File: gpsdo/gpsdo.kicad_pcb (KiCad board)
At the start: 4 copper layers, 100 x 100 mm, 64 parts, among them J1 Conn_02x05_Odd_Even, J2 Barrel_Jack_Switch, J4 USB_B_Micro, J5 Conn_01x02_Male, SW1 pushbutton_switch, SW2 SW_SPDT, U1 STM32F407VETx, U2 ATGM336H-5N, U3 AP1117-33, U4 74AHC1G04-newfp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

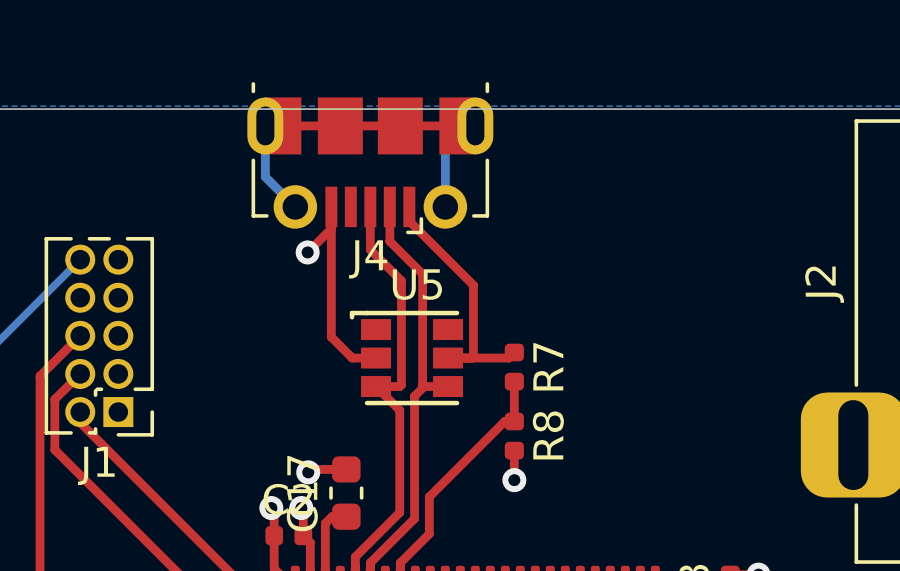
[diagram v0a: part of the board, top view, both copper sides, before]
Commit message: usb connector
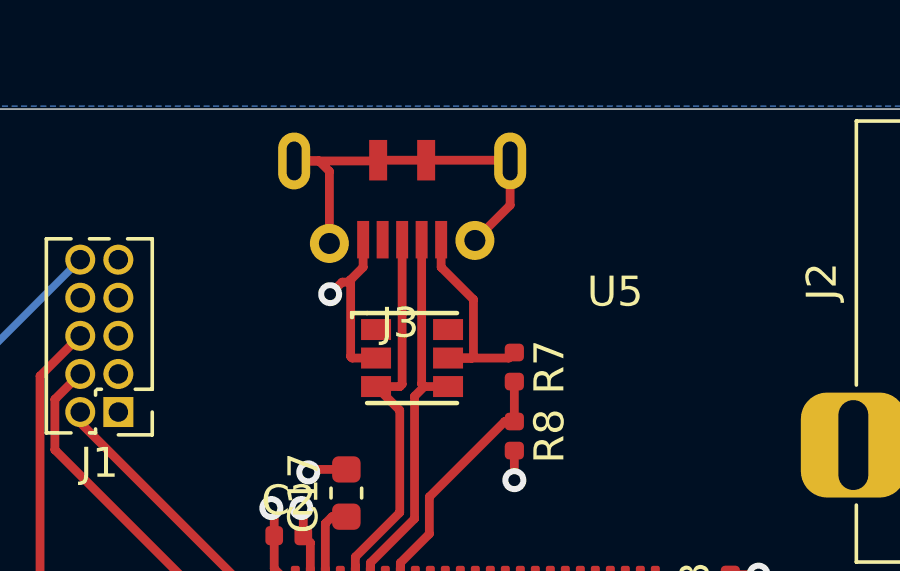
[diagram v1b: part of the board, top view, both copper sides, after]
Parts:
- removed J4: USB_B_Micro, Connector_USB:USB_Micro-B_Molex-105017-0001
- added J3: usb-micro-jlc, pace:usb-micro-jlc, F.Cu at (48.5, -0.02)
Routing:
- net Net-(J3-Pad6): track 0.00 -> 14.1 mm
- net Net-(J4-Pad6): track 13.2 -> 0.00 mm
- net GND: track 99.9 -> 97.7 mm
- net /USB_DM: track 14.8 -> 13.2 mm
- net /VUSB: track 9.02 -> 7.49 mm
- net /USB_DP: track 15.1 -> 13.6 mm
